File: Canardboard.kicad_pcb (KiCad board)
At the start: 4 copper layers, 45.7 x 58.7 mm, 170 parts, among them IC1 SIC437DED-T1-GE3, J1 RBUS, J2 USB_C_Receptacle_USB2.0, J3 Micro_SD_Card_Det, J4 Conn_01x02_Male, J5 Conn_01x03_Male, J6 Conn_01x03_Male, J7 Conn_01x03_Male, Q1 PXP012-30QLJ, Q2 PXP012-30QLJ, Q4 PXP012-30QLJ, Q6 PXP012-30QLJ, U1 ESP32-S3, U10 MP28167GQ-A-Z, U2 SN65HVD230, U3 LTC4412xS6, U4 LTC4412xS6, U5 74AHC1G00, U6 74AHC1G08, U7 ICM-20608-G, U8 MMC5983MA, U9 SC4215, Y1 40MHz±10ppm

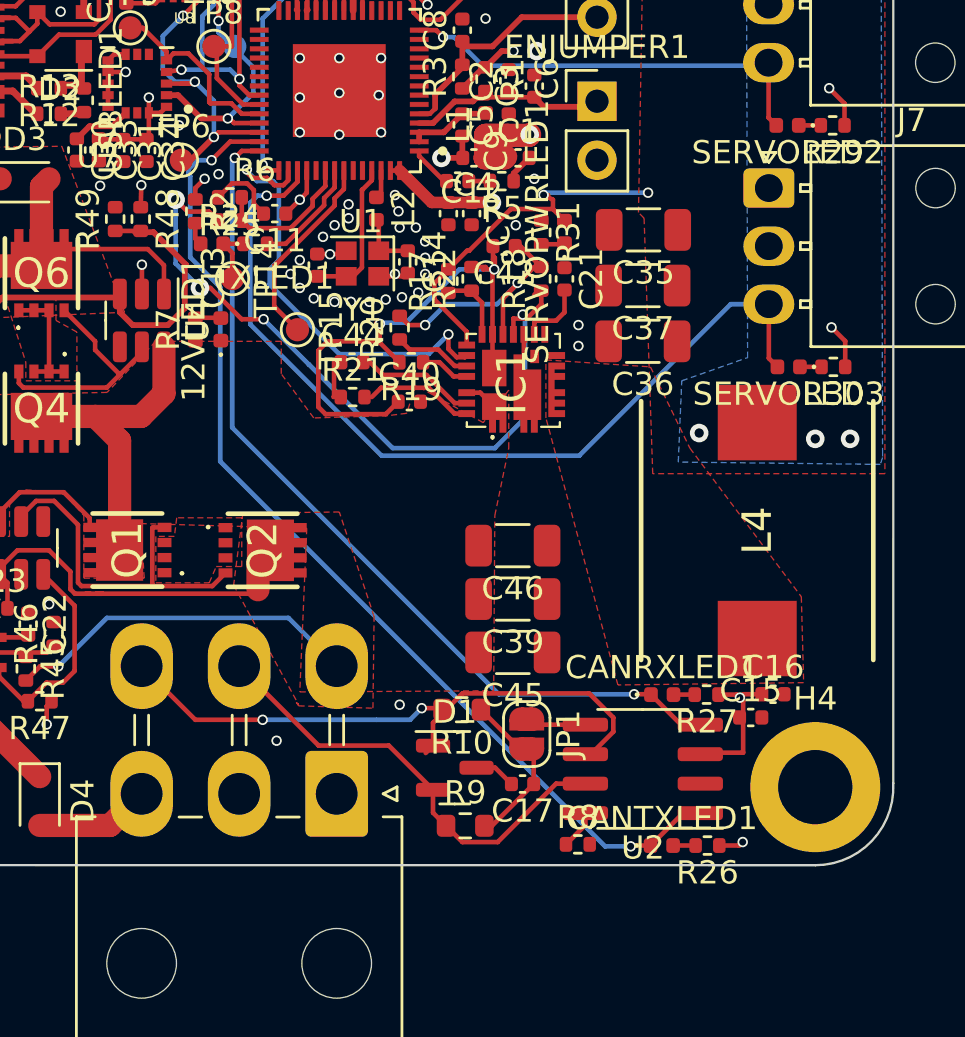
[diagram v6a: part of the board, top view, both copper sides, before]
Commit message: latest channges
dont understand why making more copper is good for thermal
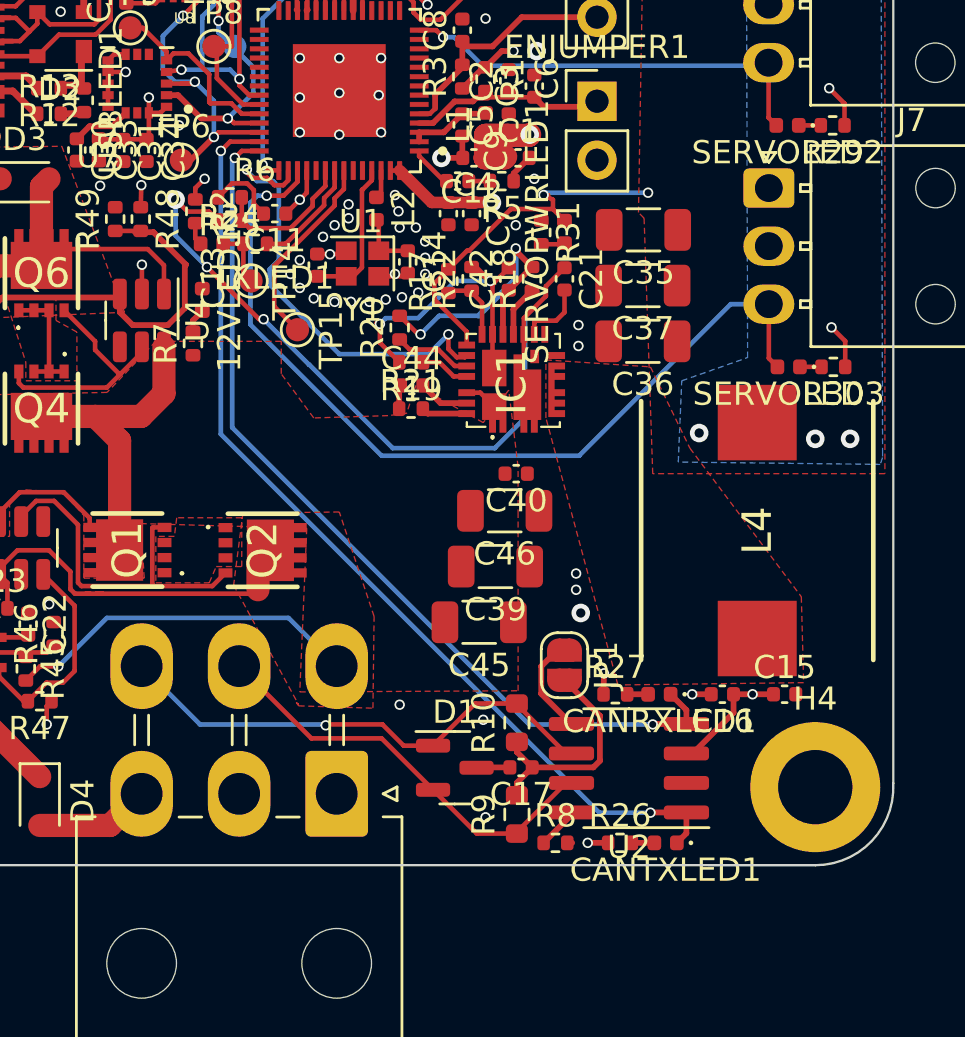
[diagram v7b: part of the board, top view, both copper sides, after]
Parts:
- moved C40 5.55 mm to (130.1, 113.5), turned to 180 degrees
- moved R27 3.93 mm to (134.4, 123.0), turned to 0 degrees
- moved R26 3.77 mm to (134.6, 129.4), turned to 0 degrees
- moved JP1 3.38 mm to (132.2, 121.8)
- moved C44 2.76 mm to (125.6, 109.7)
- moved R21 2.56 mm to (125.6, 110.7)
- moved R10 2.44 mm to (130.2, 124.2), turned to 90 degrees
- moved R9 2.28 mm to (130.2, 128.2), turned to 90 degrees
- moved C16 2.18 mm to (139.0, 123.0), turned to 180 degrees
- moved C45 1.95 mm to (128.5, 119.9)
- moved C15 1.77 mm to (141.7, 123.0)
- moved C39 1.59 mm to (129.2, 117.5)
- moved C46 1.54 mm to (129.6, 115.1)
- moved 12VLED1 1.50 mm to (116.6, 106.0), turned to -90 degrees
- moved C42 1.43 mm to (129.8, 105.1), turned to 90 degrees
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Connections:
- C40 pad 1: GNDA -> GND
- C42 pad 2: GNDA -> GND
- IC1 pad 16: GNDA -> GND
- IC1 pad 25: GNDA -> GND
- R19 pad 2: GNDA -> GND
- R22 pad 2: GNDA -> GND
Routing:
- net GNDA: track 23.7 -> 0.00 mm, vias 2 -> 0
- net GND: track 42.3 -> 60.1 mm, vias 67 -> 73
- net /CAN-: track 26.8 -> 21.6 mm, vias 2 -> 1
- net Net-(JP1-B): track 7.11 -> 9.98 mm
- net Net-(IC1-PHASE): track 4.71 -> 1.98 mm
- net Net-(IC1-BOOT): track 4.89 -> 2.20 mm
- net /CAN_TX: track 44.8 -> 42.4 mm
- net /CAN-BUS/Vref: track 2.63 -> 4.31 mm
- net /servopower/PGOOD: track 31.5 -> 29.9 mm, vias 4 -> 3
- net /CAN+: track 19.7 -> 18.2 mm
- net /servopower/VDD: track 11.3 -> 12.3 mm
- net /CAN_RX: track 38.4 -> 39.3 mm
- net +3.3V: track 49.0 -> 48.7 mm, vias 23 -> 24

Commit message: all DRC fixed
andrei hih ih ihi hi hi h
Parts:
- TP9: moved to B.Cu
- moved TP9 1.55 mm to (112.0, 94.3), turned to 180 degrees
- moved SERVOPWRLED1 0.62 mm to (132.8, 102.8)
- moved R31 0.22 mm to (131.0, 103.2)
- moved J4 0.16 mm to (105.0, 108.0)
- moved D2 0.10 mm to (110.4, 94.6)
- moved Q2 0.10 mm to (119.3, 116.8)
- moved R17 0.10 mm to (127.2, 105.1)
- moved J1 0.09 mm to (122.3, 127.3)
- moved Q1 0.06 mm to (113.4, 116.8)
- moved R15 0.06 mm to (106.2, 118.9)
- moved R42 0.06 mm to (106.2, 117.0)
- moved C46 0.05 mm to (129.6, 115.2)
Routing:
- net +12V: track 20.8 -> 6.94 mm
- net /rbusmosfets/RBUS_DEPL: track 32.4 -> 23.9 mm, vias 1 -> 2
- net /servopower/PGOOD: track 29.9 -> 35.9 mm, vias 3 -> 4
- net Net-(Q1-G): track 15.6 -> 20.6 mm
- net /IMU_CS: track 8.27 -> 9.97 mm, vias 0 -> 1
- net Net-(SERVOPWRLED1-K): track 1.02 -> 2.10 mm
